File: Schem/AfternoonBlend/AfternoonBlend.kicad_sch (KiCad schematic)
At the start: 0 parts

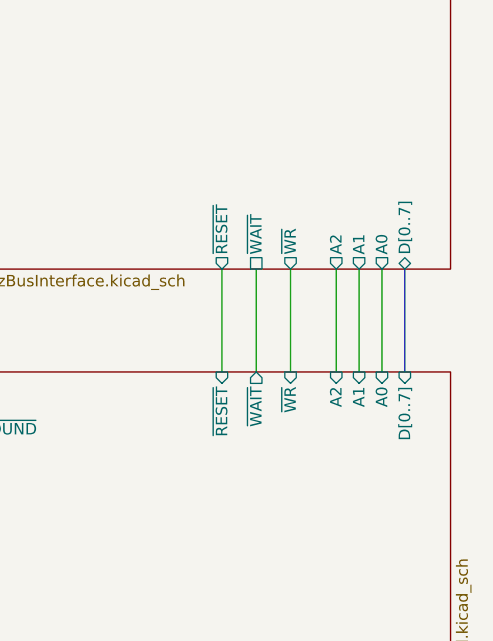
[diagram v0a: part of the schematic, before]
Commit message: Added a buffer on the Data Line to avoid overloading the CPU data bus with the 5 ICs on the board.
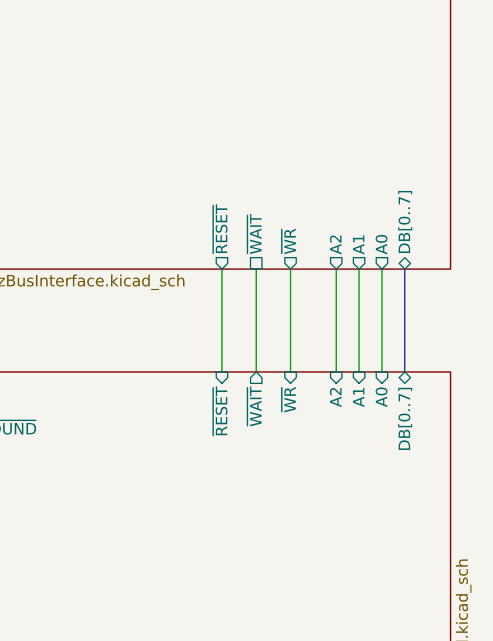
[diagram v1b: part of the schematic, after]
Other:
- sheet Sound ports: added DB[0..7]; removed D[0..7]
- sheet pBITz Bus Interface ports: added DB[0..7]; removed D[0..7]
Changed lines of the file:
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@@
-			)
-		)
-		(pin "D[0..7]" bidirectional
-			(at 152.4 91.44 270)
-			(effects
-				(font
-					(size 1.27 1.27)
-				)
-				(justify left)
 			)
 		)
@@
 		(pin "~{RESET}" output
 			(at 132.08 91.44 270)
+			(effects
+				(font
+					(size 1.27 1.27)
+				)
+				(justify left)
+			)
+		)
+		(pin "DB[0..7]" bidirectional
+			(at 152.4 91.44 270)
 			(effects
 				(font
@@
 			)
 		)
-		(pin "D[0..7]" input
-			(at 152.4 102.87 90)
+		(pin "~{RESET}" input
+			(at 132.08 102.87 90)
 			(effects
 				(font
@@
 			)
 		)
-		(pin "~{RESET}" input
-			(at 132.08 102.87 90)
+		(pin "DB[0..7]" bidirectional
+			(at 152.4 102.87 90)
 			(effects
 				(font

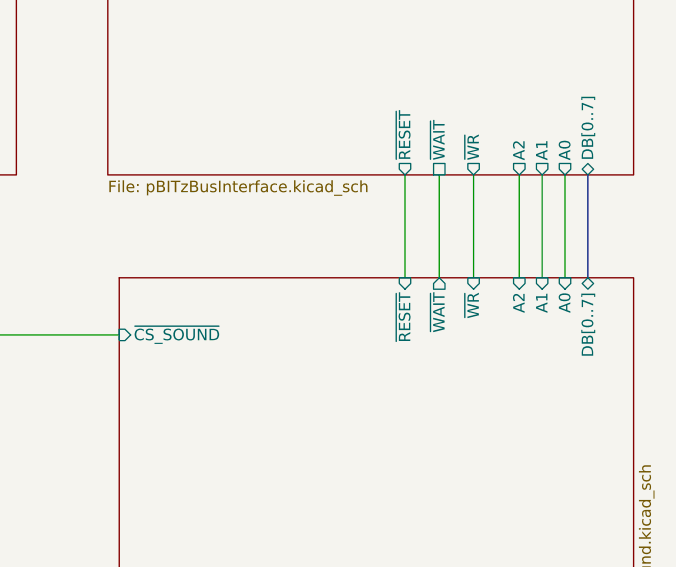
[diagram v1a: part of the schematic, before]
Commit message: Added wait-state generation to cope with a 10MHz cpu
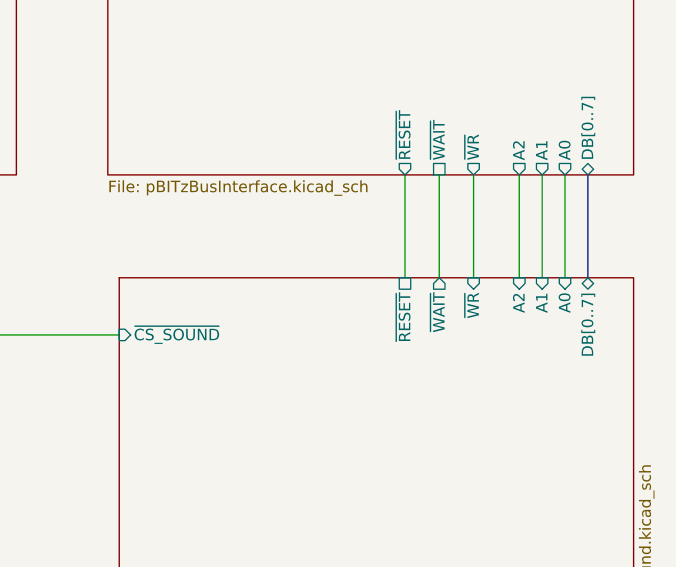
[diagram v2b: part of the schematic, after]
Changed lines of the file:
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@@
 			)
 		)
-		(pin "~{RESET}" input
+		(pin "~{RESET}" passive
 			(at 132.08 102.87 90)
 			(effects
